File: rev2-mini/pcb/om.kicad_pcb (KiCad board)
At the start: 2 copper layers, 137 x 108.8 mm, 32 parts, among them J1 Jumper

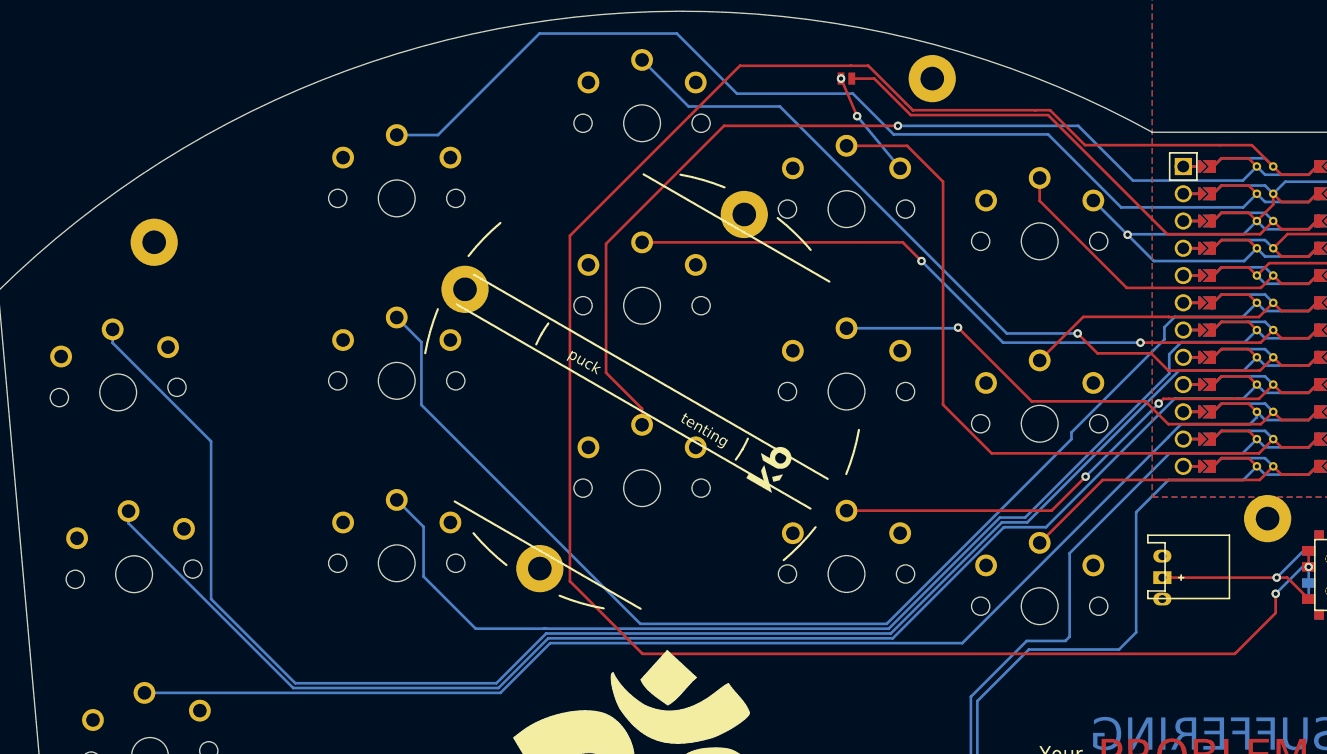
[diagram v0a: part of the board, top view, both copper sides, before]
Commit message: Finished rev2 and added a choc mini variation
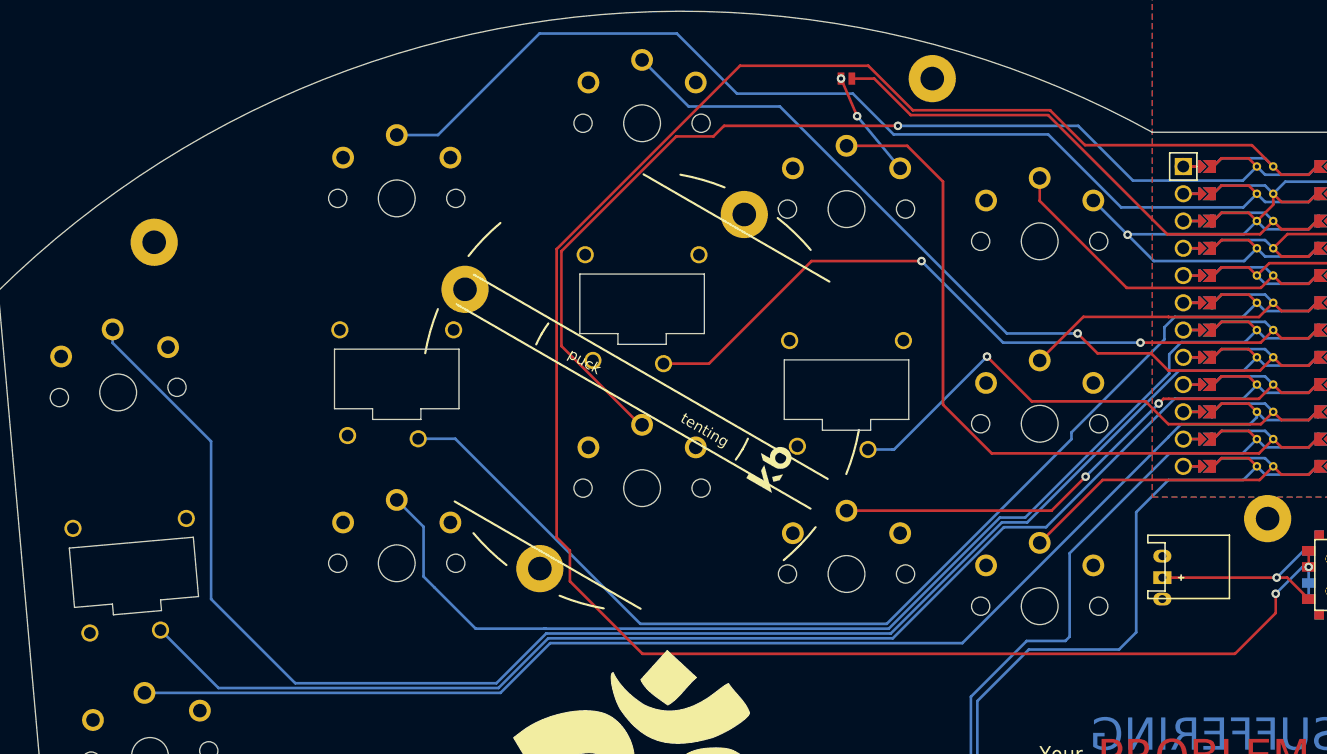
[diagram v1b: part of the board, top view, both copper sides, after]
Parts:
- S11, S2, S5, S8: footprint PG1350 -> rev2:ChocMiniSimple
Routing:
- net P3: track 108.8 -> 98.7 mm
- net P6: track 124.4 -> 116.1 mm
- net P1: track 86.1 -> 91.7 mm
- net P19: track 63.2 -> 64.4 mm
- net RAW: track 188.7 -> 189.8 mm

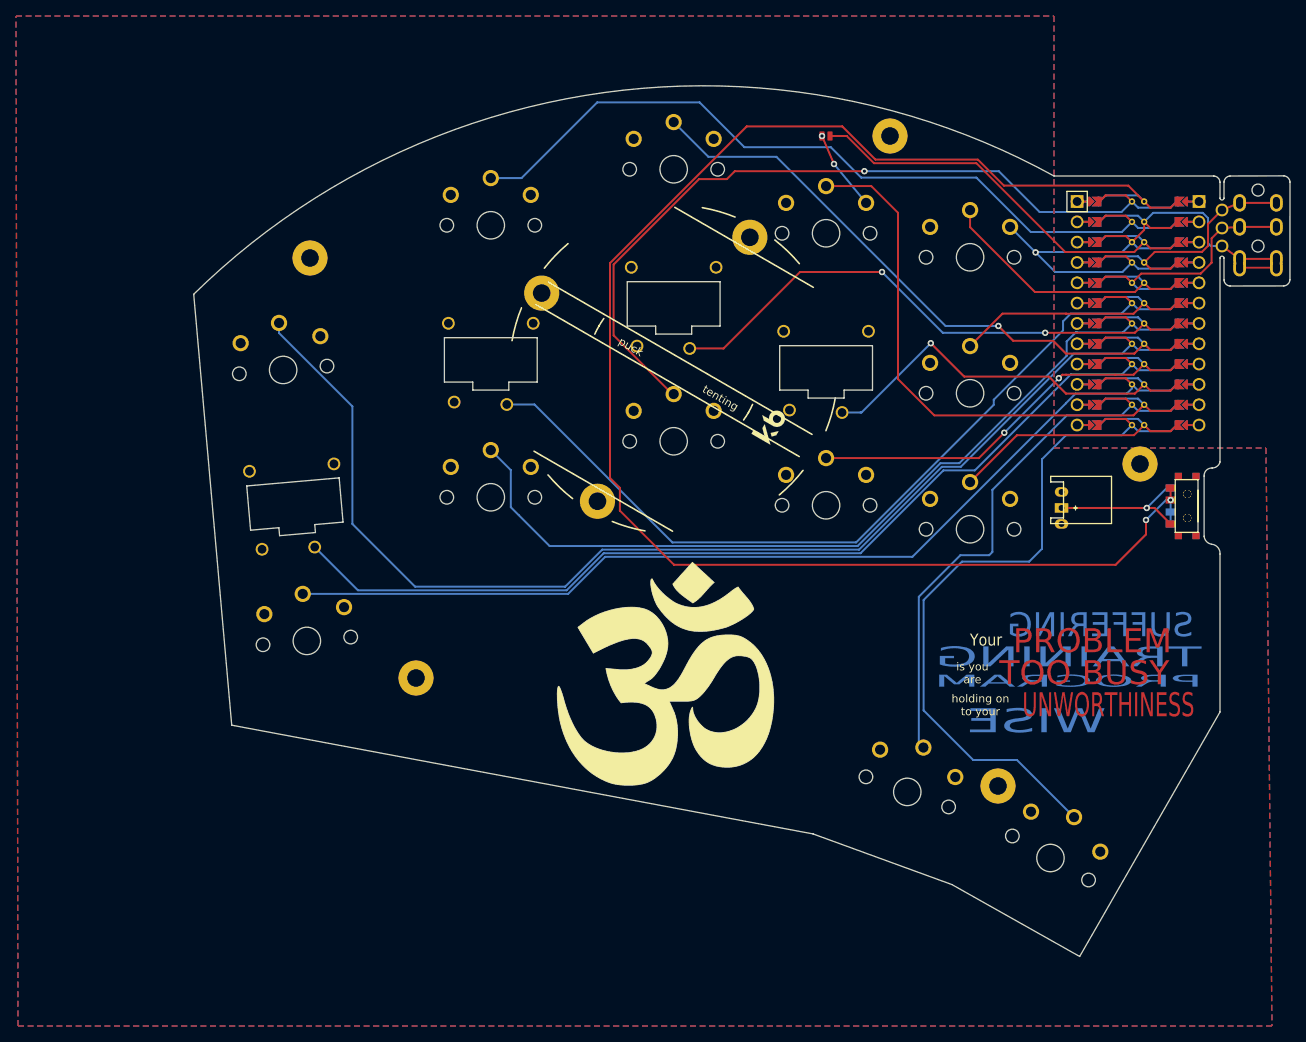
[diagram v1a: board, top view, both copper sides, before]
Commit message: Fix rev2 cutouts for on / off, add througholes for MCU cover, choc mini now has reversible mini footprints
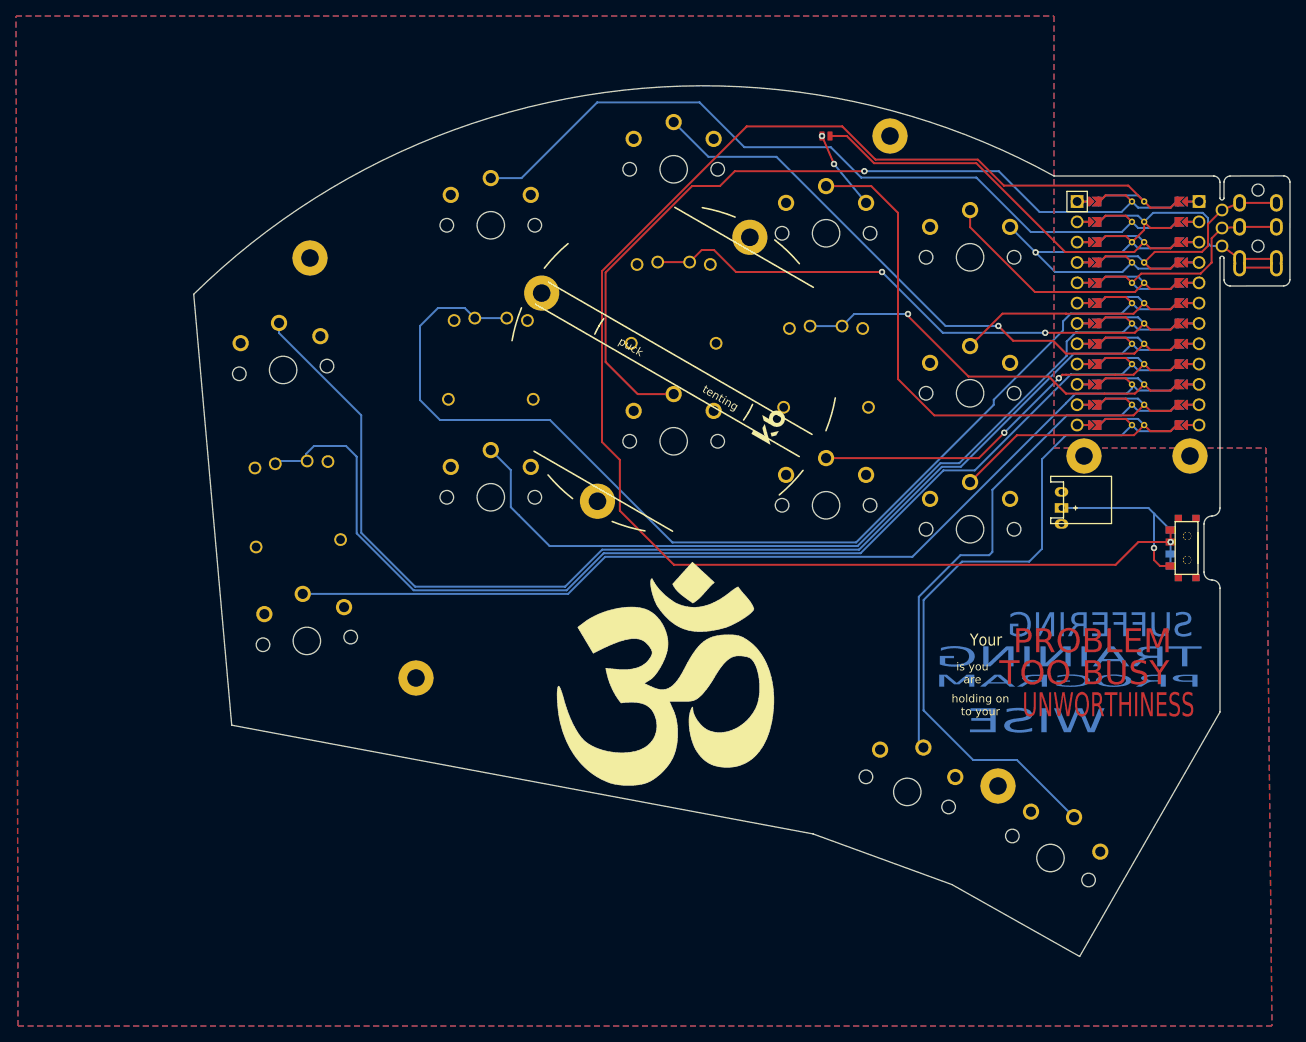
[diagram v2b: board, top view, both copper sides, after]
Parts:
- added ?: , , F.Cu at (262.7, 145.5)
- S11, S2, S5, S8: footprint rev2:ChocMiniSimple -> om:Kailh_PG1232
- moved ? 7.07 mm to (249.4, 145.5)
- moved T1 5.25 mm to (262.3, 157.0) (x2)
- turned S11 to 180 degrees
- turned S2 to -175 degrees
- turned S5 to 180 degrees
- turned S8 to 180 degrees
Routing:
- net P3: track 98.7 -> 131.4 mm
- net P6: track 116.1 -> 133.5 mm
- net POSITIVE: track 18.5 -> 22.9 mm
- net P1: track 91.7 -> 95.1 mm
- net P14: track 44.4 -> 47.1 mm
- net RAW: track 189.8 -> 187.4 mm, vias 2 -> 1
- net P19: track 64.4 -> 66.2 mm
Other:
- outline, holes or cut-outs redrawn
